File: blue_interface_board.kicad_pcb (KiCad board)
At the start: 4 copper layers, 70 x 70 mm, 124 parts, among them J1 arm connector, J2 USB_B_Micro, J3 ESTOP, J4 PWR, J5 Conn_ARM_JTAG_SWD_10, J6 logic-side RS485 debug/expans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, J7 FAN, J8 power-side RS485 debug/expans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, Q1 MMBT5401LT1G, Q2 PSMN4R8-100BSEJ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

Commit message: add part numbers, minor tweaks
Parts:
- C44: footprint Capacitor_SMD:C_0402_1005Metric -> Capacitor_SMD:C_0603_1608Metric
- R30: value 562k -> 437k; footprint Resistor_SMD:R_0402_1005Metric -> Resistor_SMD:R_0603_1608Metric
- R31: value 180k -> 140k; footprint Resistor_SMD:R_0402_1005Metric -> Resistor_SMD:R_0603_1608Metric
- moved Q2 1.50 mm to (114.0, 103.1)
- moved R27 1.50 mm to (136.3, 111.5)
- moved R28 1.50 mm to (136.3, 114.5)
- moved R9 0.70 mm to (104.5, 111.5), turned to 180 degrees
- moved D3 0.70 mm to (107.1, 109.9)
- moved Q1 0.38 mm to (101.1, 111.6)
- moved C27 0.23 mm to (102.0, 108.7)
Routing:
- net Net-(Q1-Pad1): track 3.64 -> 2.04 mm
- net Net-(R27-Pad2): track 8.33 -> 9.83 mm
- net /Power/GATE: track 13.4 -> 14.5 mm
- net GND: track 96.6 -> 96.2 mm, vias 57 -> 58

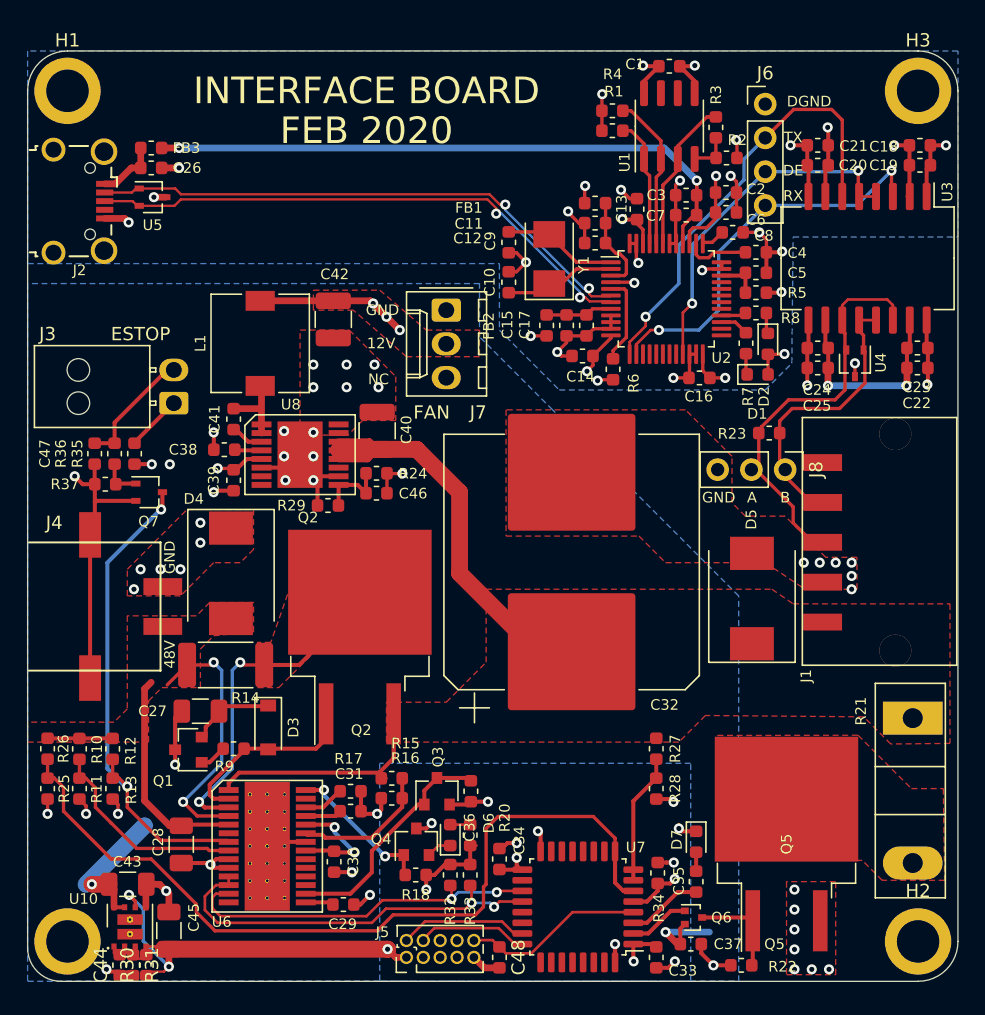
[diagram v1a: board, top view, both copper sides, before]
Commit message: add MOSFET drive IC, simply a bit by pushing more into MCU, tweak layout
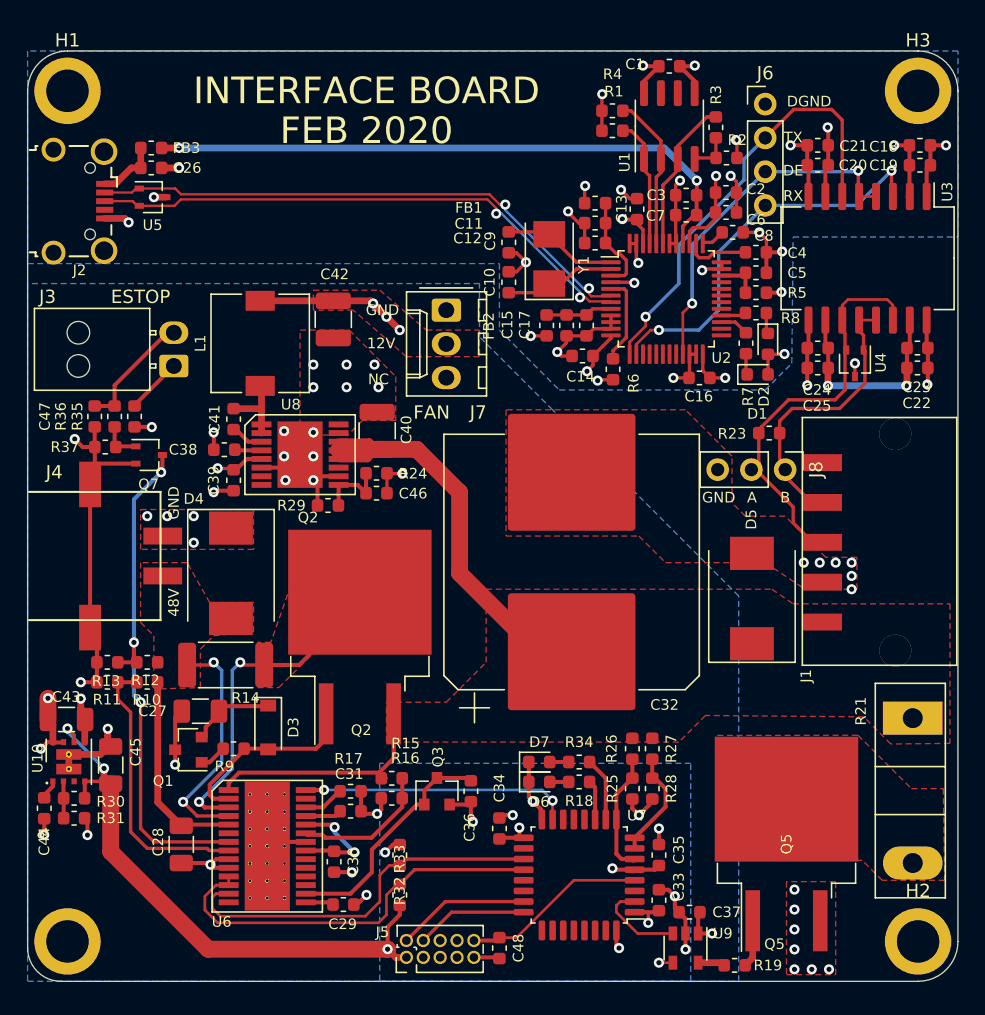
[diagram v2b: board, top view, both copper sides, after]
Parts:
- removed Q4: Q_NMOS_GDS, Package_TO_SOT_SMD:SOT-23
- removed Q6: Q_NMOS_GDS, Package_TO_SOT_SMD:SOT-416
- removed R20: 470R, Resistor_SMD:R_0603_1608Metric
- removed R22: 1k, Resistor_SMD:R_0603_1608Metric
- added R19: 33, Resistor_SMD:R_0603_1608Metric, F.Cu at (142.2, 127.8)
- added U9: FAN3111E, Package_TO_SOT_SMD:SOT-23-5, F.Cu at (138.5, 126.5)
- C37: value 100n -> 1u
- D6: value LED -> RED
- D7: value LED -> GREEN
- Q5: value Q_NMOS_GDS -> PSMN4R8-100BSEJ
- R18: value 100k -> 470R
- moved R25 44.0 mm to (134.5, 114.5)
- moved R26 44.0 mm to (134.5, 111.5)
- moved R18 14.2 mm to (130.5, 114.0)
- moved R30 13.7 mm to (92.5, 115.2), turned to 180 degrees
- moved U10 13.2 mm to (92.1, 112.5)
- moved D7 13.2 mm to (127.5, 112.5), turned to 0 degrees
- moved C43 13.2 mm to (91.9, 109.3)
- moved C45 13.2 mm to (95.2, 112.7)
- moved C44 13.1 mm to (90.2, 116.0)
- moved R34 12.6 mm to (130.5, 112.5), turned to 180 degrees
- moved R31 11.9 mm to (92.5, 116.7), turned to 0 degrees
- moved R13 9.51 mm to (95.0, 105.0), turned to 180 degrees
- moved R11 8.27 mm to (95.0, 106.5), turned to 180 degrees
- moved D6 7.80 mm to (127.5, 114.0), turned to 0 degrees
- moved R10 7.15 mm to (98.0, 106.5), turned to 180 degrees
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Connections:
- D6 pad 1: Net-(D6-Pad1) -> GND
- R18 pad 1: +3.3VP -> /Power/LEDR
- R18 pad 2: /Power/PGD -> Net-(D6-Pad2)
- R26 pad 1: /Power/VIN -> VOUT
- R34 pad 1: Net-(R34-Pad1) -> /Power/LEDG
- U7 pad 10: Net-(U7-Pad10) -> /Power/LEDG
- U7 pad 11: Net-(U7-Pad11) -> /Power/LEDR
- U7 pad 15: Net-(U7-Pad15) -> /Power/PGD
- U7 pad 3: Net-(R34-Pad1) -> Net-(U7-Pad3)
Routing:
- net Net-(R25-Pad1): track 62.9 -> 9.02 mm
- net /Power/PGD: track 11.3 -> 20.3 mm
- net +12V: track 35.7 -> 27.2 mm, vias 8 -> 9
- net /Power/VIN: track 41.2 -> 33.0 mm
- net +3.3VP: track 48.6 -> 56.7 mm, vias 7 -> 8
- net GND: track 96.2 -> 104.2 mm, vias 58 -> 53
- net Net-(R34-Pad1): track 5.68 -> 0.00 mm
- net Net-(R10-Pad2): track 15.8 -> 21.0 mm
- net /Power/LEDG: track 0.00 -> 4.83 mm
- net Net-(Q5-Pad1): track 7.29 -> 3.94 mm
- net /Power/LEDR: track 0.00 -> 3.00 mm
- net /Power/GATE_EN: track 4.58 -> 6.91 mm
- net Net-(R19-Pad1): track 0.00 -> 2.05 mm
- net Net-(D6-Pad1): track 1.90 -> 0.00 mm
- net Net-(Q7-Pad3): track 37.6 -> 39.3 mm, vias 2 -> 3
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
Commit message: layout tweaks. add debugging headers.
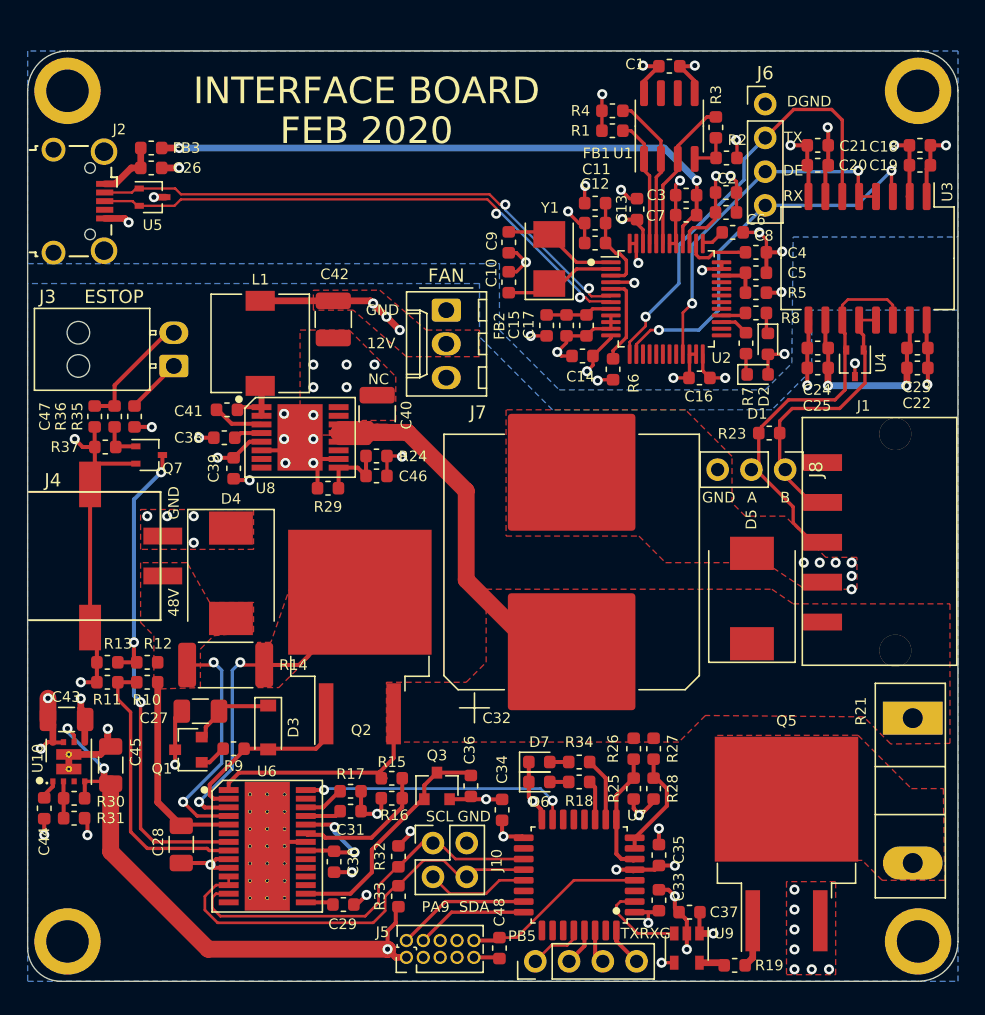
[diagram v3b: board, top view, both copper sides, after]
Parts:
- added J10: I2C, Connector_PinHeader_2.54mm:PinHeader_2x02_P2.54mm_Vertical, F.Cu at (119.5, 118.6)
- added J9: DEBUG, Connector_PinHeader_2.54mm:PinHeader_1x04_P2.54mm_Vertical, F.Cu at (127.2, 127.5)
- moved C34 1.41 mm to (124.7, 116.1)
- moved C46 1.30 mm to (115.2, 91.0)
- moved R24 1.30 mm to (115.2, 89.5)
- moved R29 1.30 mm to (111.6, 91.9)
- moved U8 1.30 mm to (109.5, 88.1)
- moved C40 1.28 mm to (115.3, 86.3)
- moved C38 0.90 mm to (103.8, 88.1)
- moved C39 0.90 mm to (104.5, 90.4)
- moved C41 0.86 mm to (104.0, 86.0), turned to 0 degrees
- moved C36 0.40 mm to (122.3, 114.3)
- moved Q3 0.40 mm to (119.8, 114.3)
- moved R32 0.14 mm to (116.9, 119.6)
- moved R33 0.14 mm to (116.9, 122.6)
- moved R25 0.10 mm to (134.6, 114.5)
- moved R26 0.10 mm to (134.6, 111.5)
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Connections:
- U7 pad 21: Net-(U7-Pad21) -> /Power/GPIO1
- U7 pad 28: Net-(U7-Pad28) -> /Power/GPIO0
- U7 pad 29: Net-(U7-Pad29) -> /Power/TX
- U7 pad 30: Net-(U7-Pad30) -> /Power/RX
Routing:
- net /Power/GPIO1: track 0.00 -> 7.76 mm
- net /Power/GPIO0: track 0.00 -> 4.23 mm
- net /Power/TX: track 0.00 -> 2.81 mm
- net /Power/RX: track 0.00 -> 2.57 mm
- net Net-(C41-Pad2): track 5.58 -> 4.19 mm
- net Net-(C41-Pad1): track 2.48 -> 3.84 mm
- net +3.3VP: track 56.7 -> 58.0 mm, vias 8 -> 9
- net VOUT: track 53.4 -> 54.3 mm
- net GND: track 104.2 -> 105.1 mm, vias 53 -> 50
- net +12V: track 27.2 -> 27.8 mm
- added copper zone on In2.Cu, net +12V
- added copper zone on In2.Cu, net +3.3VP
- added copper zone on B.Cu, net GND
- removed copper zone on B.Cu, net +12V
- removed copper zone on B.Cu, net +3.3VP
- removed copper zone on In2.Cu, net GND
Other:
- board text added: "PA9"
- board text added: "PB5"
- board text added: "SCL"
- board text added: "SDA"
- board text added: "TXRXG"

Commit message: ready to generate CAM
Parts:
- added C49: 22u, Capacitor_SMD:C_1206_3216Metric, F.Cu at (118.8, 65.1)
- added C50: 4n7, Capacitor_SMD:C_0603_1608Metric, F.Cu at (125.8, 67.1)
- added C51: 47u, Capacitor_SMD:C_1206_3216Metric, F.Cu at (122.5, 61.9)
- added R20: 437k, Resistor_SMD:R_0603_1608Metric, F.Cu at (125.0, 64.6)
- added R22: 140k, Resistor_SMD:R_0603_1608Metric, F.Cu at (126.5, 64.6)
- added U11: LMZ21700SIL, BLDC:SIL0008E, F.Cu at (122.0, 65.1)
- C29, C30: value 1uF -> 1u
- C36: value 1nF -> 1n
- C40, C42: footprint Capacitor_SMD:C_1210_3225Metric -> Capacitor_SMD:C_1206_3216Metric
- D1: value LED -> GREEN
- D2: value LED -> RED
- R11: value 6k5 -> 6k49
- R3: value 2k -> 2.2k
- U7: value STM32L011K4Tx -> STM32L071KZT6
- moved R29 4.47 mm to (115.3, 89.4)
- moved R24 2.38 mm to (116.1, 91.7), turned to 90 degrees
- moved C1 1.28 mm to (136.0, 60.1)
- moved C46 0.97 mm to (114.6, 91.7), turned to 90 degrees
- moved C40 0.20 mm to (115.1, 86.3)
- moved R9 0.10 mm to (104.4, 111.5)
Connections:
- net Net-(R7-Pad2) renamed /Comms/RXLED
- net Net-(R8-Pad2) renamed /Comms/TXLED
- C1 pad 1: +3V3 -> /Comms/FT232H_3V3
- C13 pad 1: +3V3 -> /Comms/FT232H_3V3
- C14 pad 1: +3V3 -> /Comms/FT232H_3V3
- C16 pad 1: +3V3 -> /Comms/FT232H_3V3
- C2 pad 1: +3V3 -> /Comms/FT232H_3V3
- C6 pad 1: +3V3 -> /Comms/FT232H_3V3
- D1 pad 2: +3V3 -> /Comms/FT232H_3V3
- D2 pad 2: +3V3 -> /Comms/FT232H_3V3
- FB1 pad 2: +3V3 -> /Comms/FT232H_3V3
- FB2 pad 1: +3V3 -> /Comms/FT232H_3V3
- R1 pad 1: +3V3 -> /Comms/FT232H_3V3
- R2 pad 1: +3V3 -> /Comms/FT232H_3V3
- R4 pad 1: +3V3 -> /Comms/FT232H_3V3
- R5 pad 2: +3V3 -> /Comms/FT232H_3V3
- U1 pad 8: +3V3 -> /Comms/FT232H_3V3
- U2 pad 12: +3V3 -> /Comms/FT232H_3V3
- U2 pad 24: +3V3 -> /Comms/FT232H_3V3
- U2 pad 39: +3V3 -> /Comms/FT232H_3V3
- U2 pad 46: +3V3 -> /Comms/FT232H_3V3
- U7 pad 31: Net-(U7-Pad31) -> GND
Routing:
- net /Comms/FT232H_3V3: track 0.00 -> 32.7 mm, vias 0 -> 10
- net +5V: track 46.4 -> 19.7 mm, vias 2 -> 6
- net +3V3: track 41.0 -> 25.4 mm, vias 13 -> 6
- net +12V: track 27.8 -> 40.5 mm
- net GNDD: track 57.4 -> 68.4 mm, vias 19 -> 24
- net GND: track 105.1 -> 110.0 mm, vias 50 -> 52
- net Net-(R20-Pad2): track 0.00 -> 3.07 mm
- net Net-(C50-Pad2): track 0.00 -> 1.77 mm
- net /Comms/RS485_DE: track 26.6 -> 28.3 mm
- added copper zone on F.Cu, net +3V3
- added copper zone on B.Cu, net +5V
- added copper zone on F.Cu, net +5V
- added copper zone on In2.Cu, net /Comms/FT232H_3V3
- added copper zone on F.Cu, net GNDD
